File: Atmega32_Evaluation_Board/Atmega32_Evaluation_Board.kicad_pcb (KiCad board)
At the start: 4 copper layers, 46 x 57.5 mm, 43 parts, among them J1 Barrel_Jack_Switch, J2 ICSP, SW1 RESET, U1 LM1117MP-5.0, U2 LM1117MP-3.3, U3 ATmega32A-A, Y1 16MHz

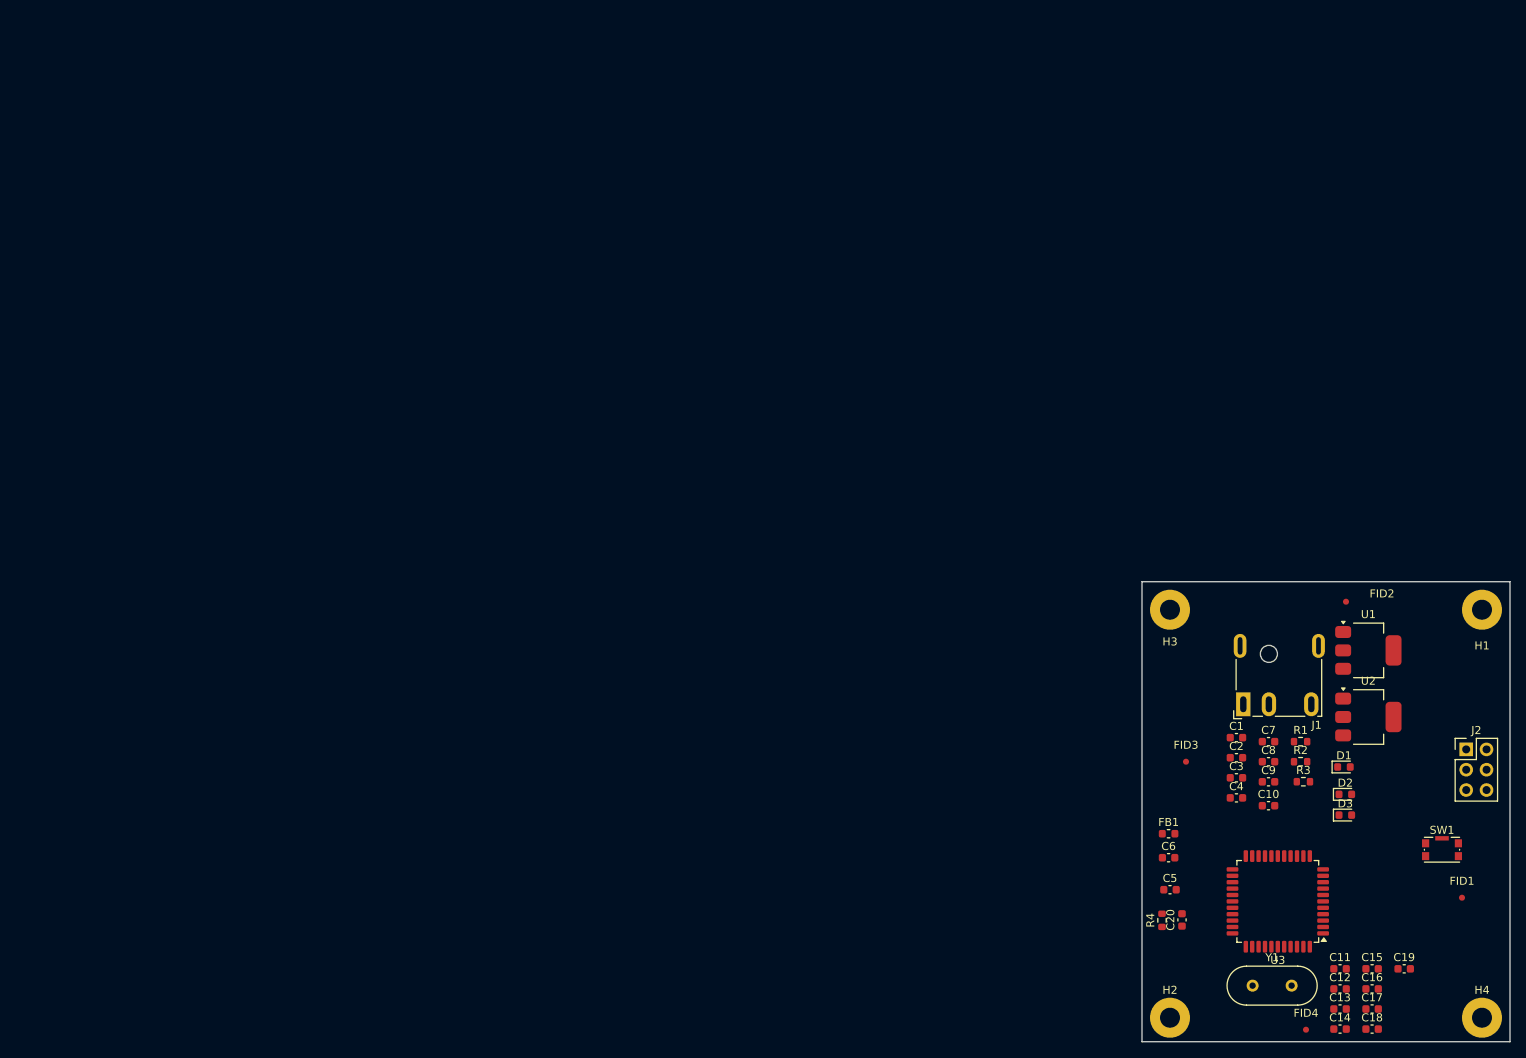
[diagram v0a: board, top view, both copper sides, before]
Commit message: added Atmega project
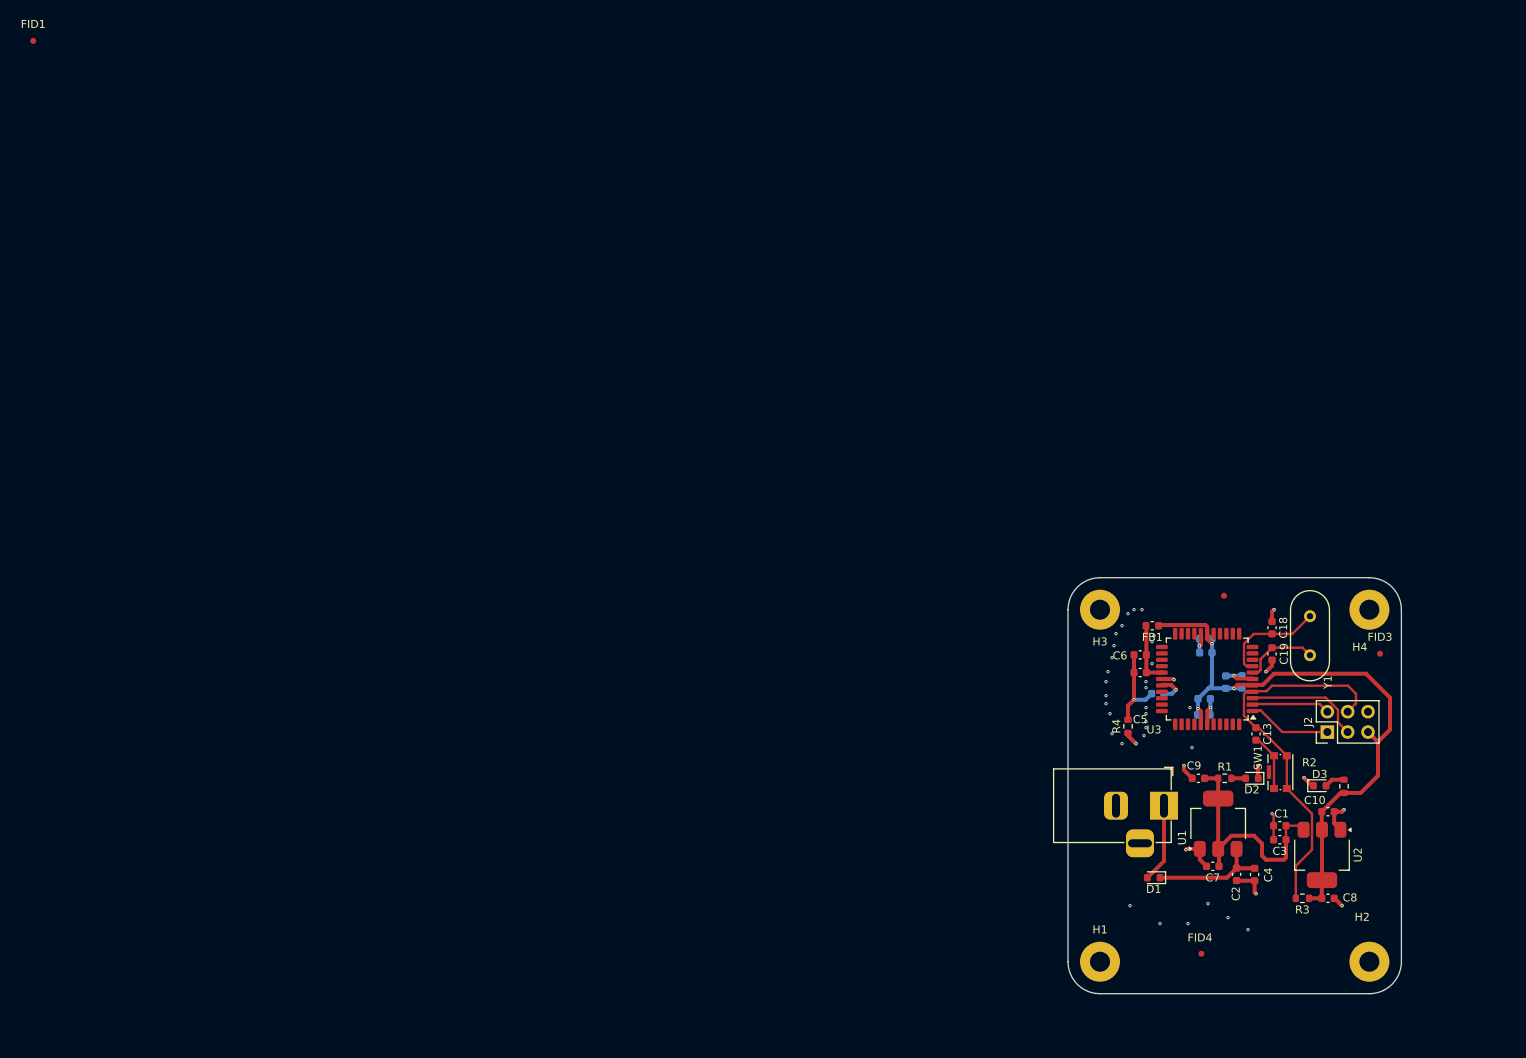
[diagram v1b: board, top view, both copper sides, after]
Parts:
- C11, C12, C14, C15, C16, C17, C20: moved to B.Cu
- J1: footprint Connector_BarrelJack:BarrelJack_CUI_PJ-079BH_Horizontal -> Connector_BarrelJack:BarrelJack_Horizontal
- moved FID1 208.3 mm to (1.40, 1.40)
- moved H1 64.9 mm to (134.8, 116.5)
- moved H4 52.9 mm to (168.4, 72.5)
- moved C18 51.7 mm to (156.2, 74.8), turned to -90 degrees
- moved C14 49.9 mm to (148.0, 77.9), turned to 180 degrees
- moved C16 48.5 mm to (148.0, 76.1), turned to 180 degrees
- moved C19 42.7 mm to (156.2, 78.0), turned to 90 degrees
- moved C17 42.4 mm to (147.7, 85.6)
- moved Y1 41.9 mm to (161.0, 78.2), turned to 90 degrees
- moved C15 40.2 mm to (150.5, 81.5), turned to 90 degrees
- moved C12 40.0 mm to (147.8, 83.6)
- moved C11 37.9 mm to (152.5, 81.5), turned to 90 degrees
- moved C13 36.0 mm to (154.2, 88.0), turned to -90 degrees
- moved U3 29.2 mm to (148.2, 81.2)
- moved U1 28.7 mm to (149.5, 99.2), turned to 90 degrees
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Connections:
- net Net-(D1-K) renamed /Power/9VD
- net Net-(U3-AREF) renamed /Microcontroller/AREF
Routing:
- net +3V3D: track 0.00 -> 80.1 mm, vias 0 -> 3
- net RST: track 0.00 -> 47.6 mm
- net GNDD: track 0.00 -> 40.8 mm, vias 0 -> 47
- net +5VD: track 0.00 -> 30.5 mm
- net /Power/9VD: track 0.00 -> 14.7 mm
- net PB7: track 0.00 -> 14.6 mm
- net Net-(U3-XTAL1): track 0.00 -> 13.4 mm
- net GNDA: track 0.00 -> 10.9 mm, vias 0 -> 1
- net PB5: track 0.00 -> 10.5 mm
- net +9VD: track 0.00 -> 9.86 mm
- net PB6: track 0.00 -> 9.73 mm
- net Net-(U3-XTAL2): track 0.00 -> 9.61 mm
- net +3V3A: track 0.00 -> 7.87 mm
- net Net-(C13-Pad2): track 0.00 -> 7.16 mm
- net /Microcontroller/AREF: track 0.05 -> 3.70 mm, vias 0 -> 1
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- added copper zone on In1.Cu, net GNDD
- added copper zone on In2.Cu, net GNDD
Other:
- board size 46 x 57.5 mm -> 41.7 x 52 mm
